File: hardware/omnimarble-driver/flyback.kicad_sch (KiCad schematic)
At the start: 9 parts, among them J5 COIL

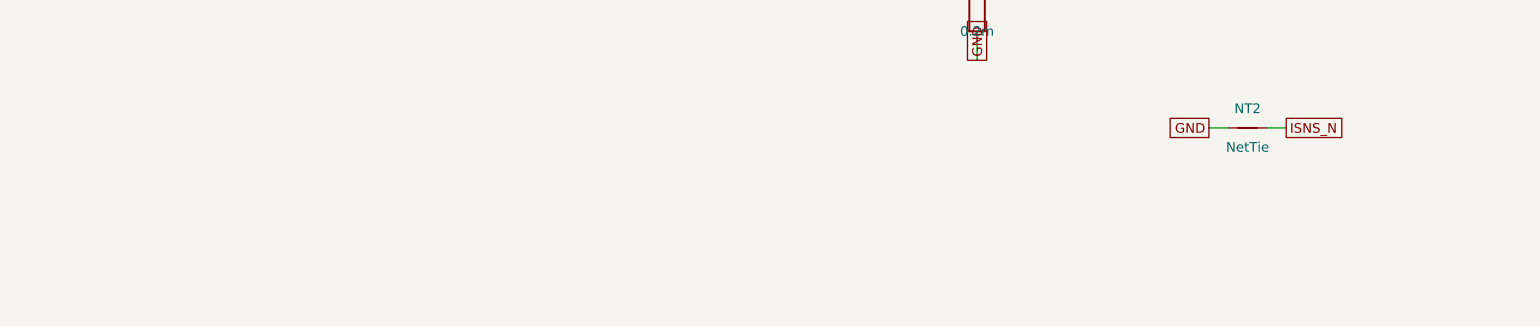
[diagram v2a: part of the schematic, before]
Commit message: Coil safety envelope, schematic coil-requirements note, 55V optimizer run
Follow-ups from the hardware review:

1. calcs.py now sweeps coil (L_uH x R_total) at the worst configuration
   (11000uF bank @ 55V) against the pulse margins (I_pk<=600A, FET dTj,
   diode I2t, pour heating, ADC FS) and derives a conservative
   rectangular envelope: **L >= 1uH AND R_total >= 90 mOhm** (resistance
   dominates at 55V: V/R at 90 mOhm ~ the 600A design point). Full
   safe/unsafe grid emitted to design-calcs.md; machine-readable
   envelope in hardware/coil-envelope.json; asserts that the rectangle
   exists and that the demo coil (12.4uH/110 mOhm) is inside.
2. Flyback sheet now carries a COIL REQUIREMENTS note next to J5,
   sourced from coil-envelope.json at generation time (no magic
   numbers; calcs.py runs before gen_schematic.py).
3. hardware/README.md created with a "Supported coils" section: the
   demo coil as validated default (sim-comparable), the envelope rule,
   and the board-constrained optimizer recommendation. Explicit note
   that the old 396V/247J optimizer result is not a recommendation for
   this board.
4. optimize_coil_design.py gained --max-voltage/--max-current;
   ran at 55V/600A: recommended 75T AWG18 3-layer coil (49.4uH,
   129 mOhm) at ~51V/3700uF -> 228A/1.6ms/4.8J, predicted +1.0 m/s
   boost. Inside the envelope with 2.6x current margin. Results JSON
   committed.

Verification: calcs 20/20 margins pass (incl. 2 new envelope checks),
ERC 0, netlist assertions pass, validate PASS (review mode), 27 tests
green, PDFs refreshed.

Co-Authored-By: Claude Fable 5 <noreply@anthropic.com>
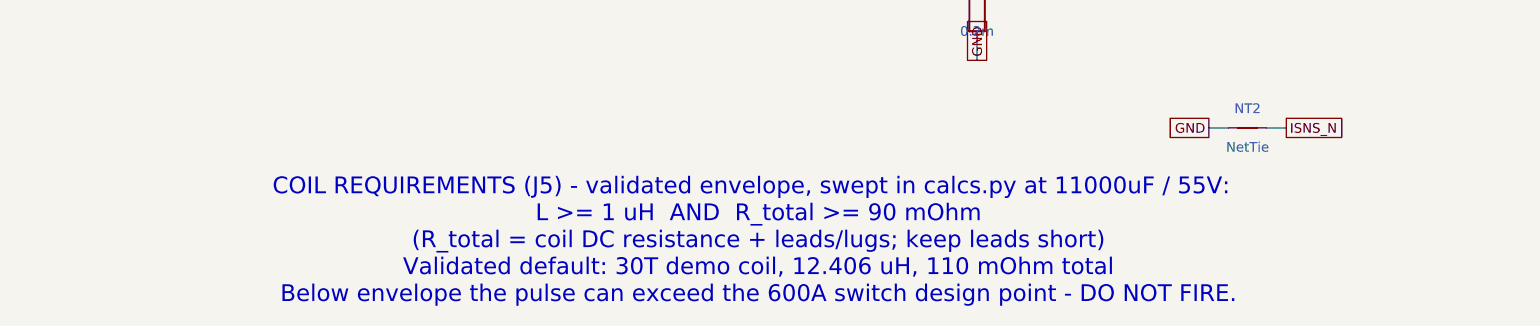
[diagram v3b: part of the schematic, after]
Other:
- note added: "COIL REQUIREMENTS (J5) - validated envelope, swept in calcs.py at 11000uF / 55V: L >= 1 uH AND R_total >= 90 mOhm (R_total = coil DC resistance + leads/lugs; keep leads short) Validated default: 30T demo coil, 12.406 uH, 110 mOhm total Below envelope the pulse can exceed the 600A switch design point - DO NOT FIRE."
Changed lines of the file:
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@@
+		)
+	)
+	(text "COIL REQUIREMENTS (J5) - validated envelope, swept in calcs.py at 11000uF / 55V:\n  L >= 1 uH  AND  R_total >= 90 mOhm\n  (R_total = coil DC resistance + leads/lugs; keep leads short)\n  Validated default: 30T demo coil, 12.406 uH, 110 mOhm total\n  Below envelope the pulse can exceed the 600A switch design point - DO NOT FIRE."
+		(exclude_from_sim no)
+		(at 30 180 0)
+		(effects
+			(font
+				(size 2.2 2.2)
+			)
 		)
 	)
@@
 		(instances
 			(project "omnimarble-driver"
-				(path "/c89355ad-4adf-4b5c-899e-310d503107ce/ab0c8335-ffa8-4763-93f4-a201ab2cd720"
+				(path "/70e4f6fa-a16c-43fd-8b02-c5feb48cd6d1/e794e164-51c0-4cba-b7e4-a825b7ab67dd"
 					(reference "D9")
 					(unit 1)
@@
 		(instances
 			(project "omnimarble-driver"
-				(path "/c89355ad-4adf-4b5c-899e-310d503107ce/ab0c8335-ffa8-4763-93f4-a201ab2cd720"
+				(path "/70e4f6fa-a16c-43fd-8b02-c5feb48cd6d1/e794e164-51c0-4cba-b7e4-a825b7ab67dd"
 					(reference "D10")
 					(unit 1)
@@
 		(instances
 			(project "omnimarble-driver"
-				(path "/c89355ad-4adf-4b5c-899e-310d503107ce/ab0c8335-ffa8-4763-93f4-a201ab2cd720"
+				(path "/70e4f6fa-a16c-43fd-8b02-c5feb48cd6d1/e794e164-51c0-4cba-b7e4-a825b7ab67dd"
 					(reference "J5")
 					(unit 1)
@@
 		(instances
 			(project "omnimarble-driver"
-				(path "/c89355ad-4adf-4b5c-899e-310d503107ce/ab0c8335-ffa8-4763-93f4-a201ab2cd720"
+				(path "/70e4f6fa-a16c-43fd-8b02-c5feb48cd6d1/e794e164-51c0-4cba-b7e4-a825b7ab67dd"
 					(reference "D11")
 					(unit 1)
@@
 		(instances
 			(project "omnimarble-driver"
-				(path "/c89355ad-4adf-4b5c-899e-310d503107ce/ab0c8335-ffa8-4763-93f4-a201ab2cd720"
+				(path "/70e4f6fa-a16c-43fd-8b02-c5feb48cd6d1/e794e164-51c0-4cba-b7e4-a825b7ab67dd"
 					(reference "D12")
 					(unit 1)
@@
 		(instances
 			(project "omnimarble-driver"
-				(path "/c89355ad-4adf-4b5c-899e-310d503107ce/ab0c8335-ffa8-4763-93f4-a201ab2cd720"
+				(path "/70e4f6fa-a16c-43fd-8b02-c5feb48cd6d1/e794e164-51c0-4cba-b7e4-a825b7ab67dd"
 					(reference "D13")
 					(unit 1)
@@
 		(instances
 			(project "omnimarble-driver"
-				(path "/c89355ad-4adf-4b5c-899e-310d503107ce/ab0c8335-ffa8-4763-93f4-a201ab2cd720"
+				(path "/70e4f6fa-a16c-43fd-8b02-c5feb48cd6d1/e794e164-51c0-4cba-b7e4-a825b7ab67dd"
 					(reference "RS1")
 					(unit 1)
@@
 		(instances
 			(project "omnimarble-driver"
-				(path "/c89355ad-4adf-4b5c-899e-310d503107ce/ab0c8335-ffa8-4763-93f4-a201ab2cd720"
+				(path "/70e4f6fa-a16c-43fd-8b02-c5feb48cd6d1/e794e164-51c0-4cba-b7e4-a825b7ab67dd"
 					(reference "NT1")
 					(unit 1)
@@
 		(instances
 			(project "omnimarble-driver"
-				(path "/c89355ad-4adf-4b5c-899e-310d503107ce/ab0c8335-ffa8-4763-93f4-a201ab2cd720"
+				(path "/70e4f6fa-a16c-43fd-8b02-c5feb48cd6d1/e794e164-51c0-4cba-b7e4-a825b7ab67dd"
 					(reference "NT2")
 					(unit 1)
@@
 		(instances
 			(project "omnimarble-driver"
-				(path "/c89355ad-4adf-4b5c-899e-310d503107ce/ab0c8335-ffa8-4763-93f4-a201ab2cd720"
+				(path "/70e4f6fa-a16c-43fd-8b02-c5feb48cd6d1/e794e164-51c0-4cba-b7e4-a825b7ab67dd"
 					(reference "#PWR0014")
 					(unit 1)

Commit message: Datasheet-exact footprints, placement engine, scripted PCB router WIP
- gen_footprints.py: TOLL-8, D2PAK (cathode-tab corrected), 5930 shunt,
  9.5mm barrier, HF3FF relay land patterns; drop _DRAFT footprints
- placement.py: 220x150 board plan, pulse zone polygons derived from
  package pad windows, shelf-packed clusters, Kelvin/manual tracks
- gen_pcb.py: netlist->board generator with zone builder, via stitching,
  pad-in-zone assertions, straggler/GND-drop/escape pre-routes and a
  negotiated-congestion (PathFinder-lite) signal router + greedy cleanup
- debug_route.py/debug_map.py/debug_j7.py: router diagnostics

Co-Authored-By: Claude Fable 5 <noreply@anthropic.com>
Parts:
- D10, D11, D12, D13, D9: footprint Package_TO_SOT_SMD:TO-263-2 -> omnimarble:D2PAK_MBR60100DC
- J5: footprint omnimarble:TerminalBarrier_1x02_P9.50mm_DRAFT -> omnimarble:TerminalBarrier_1x02_P9.50mm
- RS1: footprint omnimarble:Shunt_5930_DRAFT -> omnimarble:Shunt_5930
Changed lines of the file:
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@@
 			)
 		)
-		(property "Footprint" "Package_TO_SOT_SMD:TO-263-2"
+		(property "Footprint" "omnimarble:D2PAK_MBR60100DC"
 			(at 49.53 59.69 0)
 			(show_name no)
@@
 		(instances
 			(project "omnimarble-driver"
-				(path "/70e4f6fa-a16c-43fd-8b02-c5feb48cd6d1/e794e164-51c0-4cba-b7e4-a825b7ab67dd"
+				(path "/be74192f-67ac-494b-9ef4-1b59d4ce9fe4/08effd15-21f5-42bf-a9ba-5c59568dee55"
 					(reference "D9")
 					(unit 1)
@@
 			)
 		)
-		(property "Footprint" "Package_TO_SOT_SMD:TO-263-2"
+		(property "Footprint" "omnimarble:D2PAK_MBR60100DC"
 			(at 80.01 59.69 0)
 			(show_name no)
@@
 		(instances
 			(project "omnimarble-driver"
-				(path "/70e4f6fa-a16c-43fd-8b02-c5feb48cd6d1/e794e164-51c0-4cba-b7e4-a825b7ab67dd"
+				(path "/be74192f-67ac-494b-9ef4-1b59d4ce9fe4/08effd15-21f5-42bf-a9ba-5c59568dee55"
 					(reference "D10")
 					(unit 1)
@@
 			)
 		)
-		(property "Footprint" "omnimarble:TerminalBarrier_1x02_P9.50mm_DRAFT"
+		(property "Footprint" "omnimarble:TerminalBarrier_1x02_P9.50mm"
 			(at 129.54 59.69 0)
 			(show_name no)
@@
 		(instances
 			(project "omnimarble-driver"
-				(path "/70e4f6fa-a16c-43fd-8b02-c5feb48cd6d1/e794e164-51c0-4cba-b7e4-a825b7ab67dd"
+				(path "/be74192f-67ac-494b-9ef4-1b59d4ce9fe4/08effd15-21f5-42bf-a9ba-5c59568dee55"
 					(reference "J5")
 					(unit 1)
@@
 			)
 		)
-		(property "Footprint" "Package_TO_SOT_SMD:TO-263-2"
+		(property "Footprint" "omnimarble:D2PAK_MBR60100DC"
 			(at 49.53 100.33 0)
 			(show_name no)
@@
 		(instances
 			(project "omnimarble-driver"
-				(path "/70e4f6fa-a16c-43fd-8b02-c5feb48cd6d1/e794e164-51c0-4cba-b7e4-a825b7ab67dd"
+				(path "/be74192f-67ac-494b-9ef4-1b59d4ce9fe4/08effd15-21f5-42bf-a9ba-5c59568dee55"
 					(reference "D11")
 					(unit 1)
@@
 			)
 		)
-		(property "Footprint" "Package_TO_SOT_SMD:TO-263-2"
+		(property "Footprint" "omnimarble:D2PAK_MBR60100DC"
 			(at 80.01 100.33 0)
 			(show_name no)
@@
 		(instances
 			(project "omnimarble-driver"
-				(path "/70e4f6fa-a16c-43fd-8b02-c5feb48cd6d1/e794e164-51c0-4cba-b7e4-a825b7ab67dd"
+				(path "/be74192f-67ac-494b-9ef4-1b59d4ce9fe4/08effd15-21f5-42bf-a9ba-5c59568dee55"
 					(reference "D12")
 					(unit 1)
@@
 			)
 		)
-		(property "Footprint" "Package_TO_SOT_SMD:TO-263-2"
+		(property "Footprint" "omnimarble:D2PAK_MBR60100DC"
 			(at 129.54 100.33 0)
 			(show_name no)
@@
 		(instances
 			(project "omnimarble-driver"
-				(path "/70e4f6fa-a16c-43fd-8b02-c5feb48cd6d1/e794e164-51c0-4cba-b7e4-a825b7ab67dd"
+				(path "/be74192f-67ac-494b-9ef4-1b59d4ce9fe4/08effd15-21f5-42bf-a9ba-5c59568dee55"
 					(reference "D13")
 					(unit 1)
@@
 			)
 		)
-		(property "Footprint" "omnimarble:Shunt_5930_DRAFT"
+		(property "Footprint" "omnimarble:Shunt_5930"
 			(at 59.69 149.86 0)
 			(show_name no)
@@
 		(instances
 			(project "omnimarble-driver"
-				(path "/70e4f6fa-a16c-43fd-8b02-c5feb48cd6d1/e794e164-51c0-4cba-b7e4-a825b7ab67dd"
+				(path "/be74192f-67ac-494b-9ef4-1b59d4ce9fe4/08effd15-21f5-42bf-a9ba-5c59568dee55"
 					(reference "RS1")
 					(unit 1)
@@
 		(instances
 			(project "omnimarble-driver"
-				(path "/70e4f6fa-a16c-43fd-8b02-c5feb48cd6d1/e794e164-51c0-4cba-b7e4-a825b7ab67dd"
+				(path "/be74192f-67ac-494b-9ef4-1b59d4ce9fe4/08effd15-21f5-42bf-a9ba-5c59568dee55"
 					(reference "NT1")
 					(unit 1)
@@
 		(instances
 			(project "omnimarble-driver"
-				(path "/70e4f6fa-a16c-43fd-8b02-c5feb48cd6d1/e794e164-51c0-4cba-b7e4-a825b7ab67dd"
+				(path "/be74192f-67ac-494b-9ef4-1b59d4ce9fe4/08effd15-21f5-42bf-a9ba-5c59568dee55"
 					(reference "NT2")
 					(unit 1)
@@
 		(instances
 			(project "omnimarble-driver"
-				(path "/70e4f6fa-a16c-43fd-8b02-c5feb48cd6d1/e794e164-51c0-4cba-b7e4-a825b7ab67dd"
+				(path "/be74192f-67ac-494b-9ef4-1b59d4ce9fe4/08effd15-21f5-42bf-a9ba-5c59568dee55"
 					(reference "#PWR0014")
 					(unit 1)

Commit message: Driver PCB: fix schematic parity + correct review overclaims
Addresses external review pushback on the "DRC-clean/fab-ready" framing.

- Schematic parity now 0 (was 6): footprint DNP synced for C92-94; TP1/
  NT1/NT2 excluded from BOM in schematic (test point + Kelvin net-ties).
  kicad_sch.add_symbol gains in_bom kwarg so this can't regress.
- REVIEW_HANDOFF.md rev 2: drops "DRC-clean copper" overclaim. States
  honestly this is an iteration checkpoint, not fab-ready: 59 real
  clearance errors (near-shorts to 0.010mm on FIRE_GATED/gate/BOOST_EN_N/
  ESTOP nets), 118 unconnected incl 34 safety/control/analog. Clarifies
  board is byte-identical (sha256 ed02f3b) across e64fb78/bb3ea38/ae83ebe.
- Review dashboard: verdict banner amber "iteration checkpoint - not
  fab-ready"; clearance + unconnected reclassed as blockers; parity row
  added; agreed next gate (0 unconn / 0 clearance / 0 parity + manual
  power-loop review) replaces the open-questions block.
- ERC still 0.

Co-Authored-By: Claude Fable 5 <noreply@anthropic.com>
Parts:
- NT1, NT2: now left out of the parts list
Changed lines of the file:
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@@
 		(unit 1)
 		(exclude_from_sim no)
-		(in_bom yes)
+		(in_bom no)
 		(on_board yes)
 		(dnp no)
@@
 		(unit 1)
 		(exclude_from_sim no)
-		(in_bom yes)
+		(in_bom no)
 		(on_board yes)
 		(dnp no)

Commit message: Snapshot driver's final validated state before parking as vNext
Fold the last regeneration into the repo so the source is internally consistent
with the already-committed board/BOM (the Q90 diode->MOSFET fix + JLC cart
substitutions previously landed only in the root schematic + board):
- 7 driver schematic sub-sheets, regenerated to carry the final part numbers.
- fab/jlc/ORDER_NOTES.md — final BOM (J2/J5 C707836, R21/R22 C5110275, etc.).
- omnimarble-driver-5-rev-39.ses — the routing session import-clean rebuilds the
  board from; committing it keeps the routed board reproducible while parked.

Timestamp-only gerber/zip churn and scratch (.ses iterations, drc/erc reports,
logs) were left out. Driver stays vNext/on-hold per V0_BENCH_RIG.md.

Co-Authored-By: Claude Opus 4.8 <noreply@anthropic.com>
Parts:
- J5: LCSC C60785 -> C707836
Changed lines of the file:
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@@
 		(instances
 			(project "omnimarble-driver"
-				(path "/4f6b9534-97fd-44ae-b81e-62754cb6cba6/ae63967f-3643-4626-9e70-8021e0d440ef"
+				(path "/e983a447-c241-422e-9650-13442643de66/a9fc5635-081b-4ed4-badc-26f7b26d14d3"
 					(reference "D9")
 					(unit 1)
@@
 		(instances
 			(project "omnimarble-driver"
-				(path "/4f6b9534-97fd-44ae-b81e-62754cb6cba6/ae63967f-3643-4626-9e70-8021e0d440ef"
+				(path "/e983a447-c241-422e-9650-13442643de66/a9fc5635-081b-4ed4-badc-26f7b26d14d3"
 					(reference "D10")
 					(unit 1)
@@
 			)
 		)
-		(property "LCSC" "C60785"
+		(property "LCSC" "C707836"
 			(at 129.54 59.69 0)
 			(show_name no)
@@
 		(instances
 			(project "omnimarble-driver"
-				(path "/4f6b9534-97fd-44ae-b81e-62754cb6cba6/ae63967f-3643-4626-9e70-8021e0d440ef"
+				(path "/e983a447-c241-422e-9650-13442643de66/a9fc5635-081b-4ed4-badc-26f7b26d14d3"
 					(reference "J5")
 					(unit 1)
@@
 		(instances
 			(project "omnimarble-driver"
-				(path "/4f6b9534-97fd-44ae-b81e-62754cb6cba6/ae63967f-3643-4626-9e70-8021e0d440ef"
+				(path "/e983a447-c241-422e-9650-13442643de66/a9fc5635-081b-4ed4-badc-26f7b26d14d3"
 					(reference "D11")
 					(unit 1)
@@
 		(instances
 			(project "omnimarble-driver"
-				(path "/4f6b9534-97fd-44ae-b81e-62754cb6cba6/ae63967f-3643-4626-9e70-8021e0d440ef"
+				(path "/e983a447-c241-422e-9650-13442643de66/a9fc5635-081b-4ed4-badc-26f7b26d14d3"
 					(reference "D12")
 					(unit 1)
@@
 		(instances
 			(project "omnimarble-driver"
-				(path "/4f6b9534-97fd-44ae-b81e-62754cb6cba6/ae63967f-3643-4626-9e70-8021e0d440ef"
+				(path "/e983a447-c241-422e-9650-13442643de66/a9fc5635-081b-4ed4-badc-26f7b26d14d3"
 					(reference "D13")
 					(unit 1)
@@
 		(instances
 			(project "omnimarble-driver"
-				(path "/4f6b9534-97fd-44ae-b81e-62754cb6cba6/ae63967f-3643-4626-9e70-8021e0d440ef"
+				(path "/e983a447-c241-422e-9650-13442643de66/a9fc5635-081b-4ed4-badc-26f7b26d14d3"
 					(reference "RS1")
 					(unit 1)
@@
 		(instances
 			(project "omnimarble-driver"
-				(path "/4f6b9534-97fd-44ae-b81e-62754cb6cba6/ae63967f-3643-4626-9e70-8021e0d440ef"
+				(path "/e983a447-c241-422e-9650-13442643de66/a9fc5635-081b-4ed4-badc-26f7b26d14d3"
 					(reference "NT1")
 					(unit 1)
@@
 		(instances
 			(project "omnimarble-driver"
-				(path "/4f6b9534-97fd-44ae-b81e-62754cb6cba6/ae63967f-3643-4626-9e70-8021e0d440ef"
+				(path "/e983a447-c241-422e-9650-13442643de66/a9fc5635-081b-4ed4-badc-26f7b26d14d3"
 					(reference "NT2")
 					(unit 1)
@@
 		(instances
 			(project "omnimarble-driver"
-				(path "/4f6b9534-97fd-44ae-b81e-62754cb6cba6/ae63967f-3643-4626-9e70-8021e0d440ef"
+				(path "/e983a447-c241-422e-9650-13442643de66/a9fc5635-081b-4ed4-badc-26f7b26d14d3"
 					(reference "#PWR0014")
 					(unit 1)
